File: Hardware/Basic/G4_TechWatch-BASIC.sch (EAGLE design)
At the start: 51 parts, among them J1 FTDI_DEVICESMD, SW1 SWITCH.MOM, SW2 SWITCH.MOM, SW5 SWITCH.MOM, U2 NRF52832_MODULE_MDBT42, U4 PCF8523

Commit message: Board Completed
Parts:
- removed C19: 2.2uF, LinnesLab-Passives:CAPACITOR0402
- removed C20, C21: 4.7u, LinnesLab-Passives:CAPACITOR0603
- removed D4: (no value), LinnesLab-DiscreteSemi:SCHOTTKY-USC
- removed R13, R14, R15: 100k, LinnesLab-Passives:RESISTOR0603
- removed U4: PCF8523, LinnesLab-Clocks:PCF8523
- removed XTAL3: 32.7680kHz, LinnesLab-Clocks:CRYSTALECS-.327-12.5-12-C-TR
- added C1: 1u, LinnesLab-Passives:CAPACITOR0603
- added C3, C4: (no value), LinnesLab-Passives:CAPACITOR0603
- added D3: (no value), LinnesLab-DiscreteSemi:SCHOTTKY-USC
- added R1, R10, R2: 10k, LinnesLab-Passives:RESISTOR0603
- added U1: NRF52832_MODULE_MDBT42, LinnesLab-Microcontrollers:NRF52832_MODULE_MDBT42
- added XTAL1: 32.768kHz, LinnesLab-Clocks:CRYSTALECS-.327-12.5-12-C-TR
- C10: value 300p -> 4.7u
- C11: value 300p -> 100n
- C12: value 10u -> 10uF; device LinnesLab-Passives:CAPACITOR0805 -> LinnesLab-Passives:CAPACITOR0603
- C14: value 100n -> 2.2uF; device LinnesLab-Passives:CAPACITOR0603 -> LinnesLab-Passives:CAPACITOR0402
- C16: value 10uF -> 2.2uF; device LinnesLab-Passives:CAPACITOR0603 -> LinnesLab-Passives:CAPACITOR0402
- C18: value 2.2uF -> 1u; device LinnesLab-Passives:CAPACITOR0402 -> LinnesLab-Passives:CAPACITOR0603
- C2: value 1u -> 10u; device LinnesLab-Passives:CAPACITOR0603 -> LinnesLab-Passives:CAPACITOR0805
- C5, C6: value 1u -> 300p
- C7: value 1u -> 4.7u
- C8, C9: value (none) -> 1u
- R11: value (none) -> 10k
- R12: value 100k -> 390k
- R3: value 1k -> 100k
- R5: value 10k -> 1k
- R6: value 10k -> (none)
- R7: value 390k -> 100k
- R8, R9: value 10k -> 100k
- SW1, SW2: value SWITCH.MOM -> (none); device LinnesLab-Switches:SWITCH.MOM -> LinnesLab-Switches:SPST-PTS830GG140-COPY.1-3
- SW3, SW4: value (none) -> SWITCH.MOM; device LinnesLab-Switches:SPST-PTS830GG140-COPY.1-3 -> LinnesLab-Switches:SWITCH.MOM
- U2: value NRF52832_MODULE_MDBT42 -> PCF8523; device LinnesLab-Microcontrollers:NRF52832_MODULE_MDBT42 -> LinnesLab-Clocks:PCF8523; DIGIKEY (none) -> 568-5306-1-ND; I2C_ADDRESS (none) -> 0x68h; MFN (none) -> PCF8523T/1,118; MFN_MANUFACTURER (none) -> NXP USA Inc.
- XTAL2: value 32.768kHz -> 32.7680kHz; FREQ (none) -> 32.7680KHZ
- renumbered CHRG2 to CHRG1, CORTEX1 to DEBUG1, D5 to D2, L2 to L1, LDO2 to LDO1, LED3 to LED1, LED4 to LED2
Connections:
- net 3.3V: now also C16.2, C18.1, C2.2, C9.1, D3.C, R1.2, R10.2, R2.2, R7.2, U1.VDD; no longer C12.2, C19.2, C2.1, C6.1, D1.C, R15.2, R5.2, R8.2, R9.2, U4.VDD
- net AIN7/BATT: now also R8.1, R9.2, U1.P0.31/AIN7; no longer R13.1, R14.2, U2.P0.31/AIN7
- net CHRG.STAT: now also R3.1, U1.P0.27; no longer R12.1, U2.P0.27
- net CS.OLED: now also U1.P0.16; no longer U2.P0.16
- net D7/SD.CS: now also U1.P0.07; no longer U2.P0.07
- net DC.OLED: now also U1.P0.04/AIN2; no longer U2.P0.04/AIN2
- net DFU: now also SW1.B, U1.P0.20; no longer SW3.B, U2.P0.20
- net DTR: now also C11.1; no longer C14.1
- net FRST: now also U1.P0.22; no longer U2.P0.22
- net GND: now also C1.2, C14.1, C18.2, C2.1, C3.1, C4.2, C5.2, C7.1, R12.2, R7.1, R9.1, SW1.A, SW2.B, SW3.3, SW3.4, SW4.3, SW4.4, U1.GND@1, U1.GND@2, U1.GND@3, U1.GND@4, U2.VSS; no longer C11.2, C18.1, C19.1, C2.2, C20.2, C21.1, C5.1, C7.2, R14.1, R15.1, R7.2, SW1.3, SW1.4, SW2.3, SW2.4, SW3.A, SW4.B, U2.GND@1, U2.GND@2, U2.GND@3, U2.GND@4, U4.VSS
- net LED1: now also R4.2, U1.P0.17; no longer R3.2, U2.P0.17
- net LED2: now also R5.2, U1.P0.19; no longer R4.2, U2.P0.19
- net MISO: now also U1.P0.14; no longer U2.P0.14
- net MOSI: now also U1.P0.13; no longer U2.P0.13
- net N$1: now also R11.2; no longer R6.2
- net N$10: now also R5.1; no longer R4.1
- net N$11: now also U1.DCC; no longer U2.DCC
- net N$12: now also C1.1, U1.DEC4; no longer C7.1, U2.DEC4
- net N$13: now also C12.2; no longer C16.2
- net N$15: now also C14.2; no longer C18.2
- net N$17: now also R6.2; no longer R11.2
- net N$19: now also U2.OSCO, XTAL2.1; no longer U4.OSCO, XTAL3.1
- net N$2: now also R12.1; no longer R7.1
- net N$20: now also U2.OSCI, XTAL2.2; no longer U4.OSCI, XTAL3.2
- net N$3: now also C15.2; no longer C13.2
- net N$4: now also C3.2, U1.P0.00/XL1, XTAL1.1; no longer C8.2, U2.P0.00/XL1, XTAL2.1
- net N$5: now also C15.1; no longer C13.1
- net N$6: now also C4.1, U1.P0.01/XL2, XTAL1.2; no longer C9.1, U2.P0.01/XL2, XTAL2.2
- net N$7: now also C13.2; no longer C15.2
- net N$8: now also C13.1; no longer C15.1
- net N$9: now also R4.1; no longer R3.1
- net P0.09/NFC1: now also C5.1, U1.P0.09; no longer C11.1, U2.P0.09
- net P0.10/NFC2: now also C6.1, U1.P0.10; no longer C10.1, U2.P0.10
- net RESET: now also C11.2, D3.A, R10.1, SW2.A, U1.P0.21/RESET; no longer C14.2, D1.A, R5.1, SW4.A, U2.P0.21/RESET
- net RESET.OLED: now also U1.P0.03/AIN1; no longer U2.P0.03/AIN1
- net RXD: now also U1.P0.08; no longer U2.P0.08
- net SCK: now also U1.P0.12; no longer U2.P0.12
- net SCL: now also R2.1, U1.P0.26, U2.SCL; no longer R8.1, U2.P0.26, U4.SCL
- net SDA: now also R1.1, U1.P0.25, U2.SDA; no longer R9.1, U2.P0.25, U4.SDA
- net SW1: now also SW3.1, SW3.2, U1.P0.11; no longer SW1.1, SW1.2, U2.P0.11
- net SW2: now also SW4.1, SW4.2, U1.P0.15; no longer SW2.1, SW2.2, U2.P0.15
- net SW3: now also U1.P0.28/AIN4; no longer U2.P0.28/AIN4
- net SWCLK: now also U1.SWDCLK; no longer U2.SWDCLK
- net SWDIO: now also U1.SWDIO; no longer U2.SWDIO
- net SWO: now also U1.P0.18/SWO; no longer U2.P0.18/SWO
- net TXD: now also U1.P0.06; no longer U2.P0.06
- net VIN: now also C7.2, C8.2, D1.C, R3.2; no longer C21.2, C5.2, D4.C, R12.2
- net VLIPO: now also C10.1, D1.A, R8.2; no longer C20.1, D4.A, R13.2
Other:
- moved on the sheet: C10, C11, C12, C13, C14, C15, C16, C18, C2, C5, C6, C7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

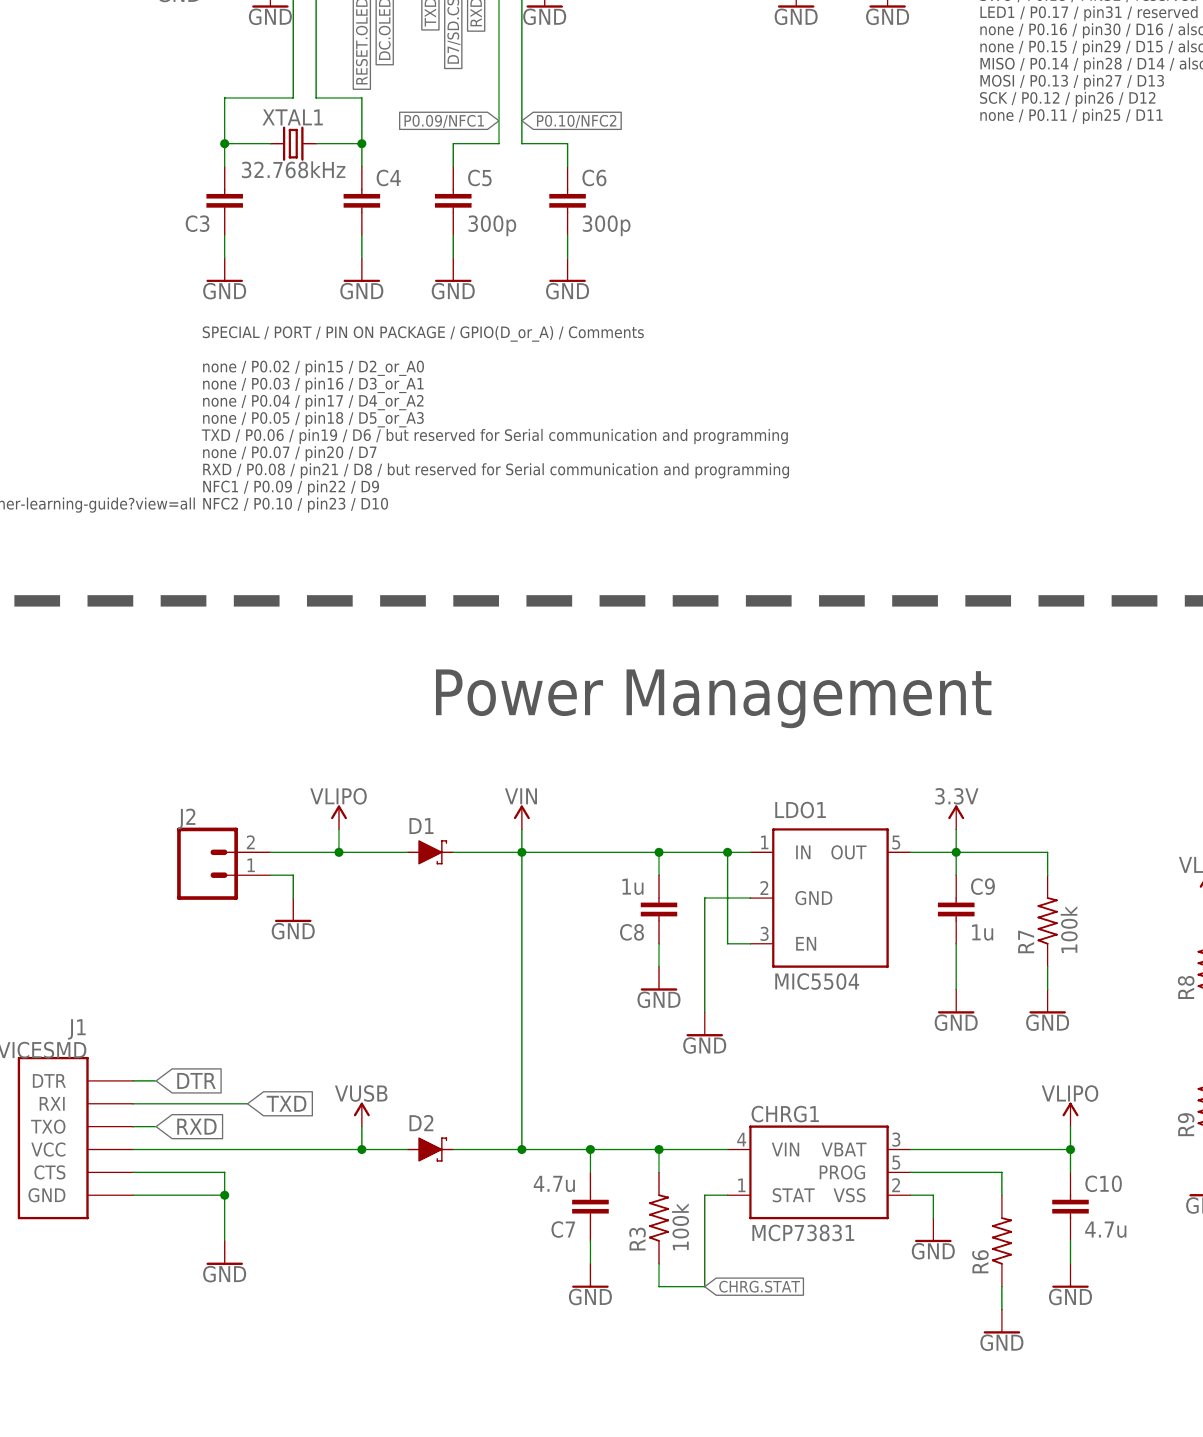
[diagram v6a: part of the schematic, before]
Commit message: Added Missing values, fixed silkscreen and OLED spacing
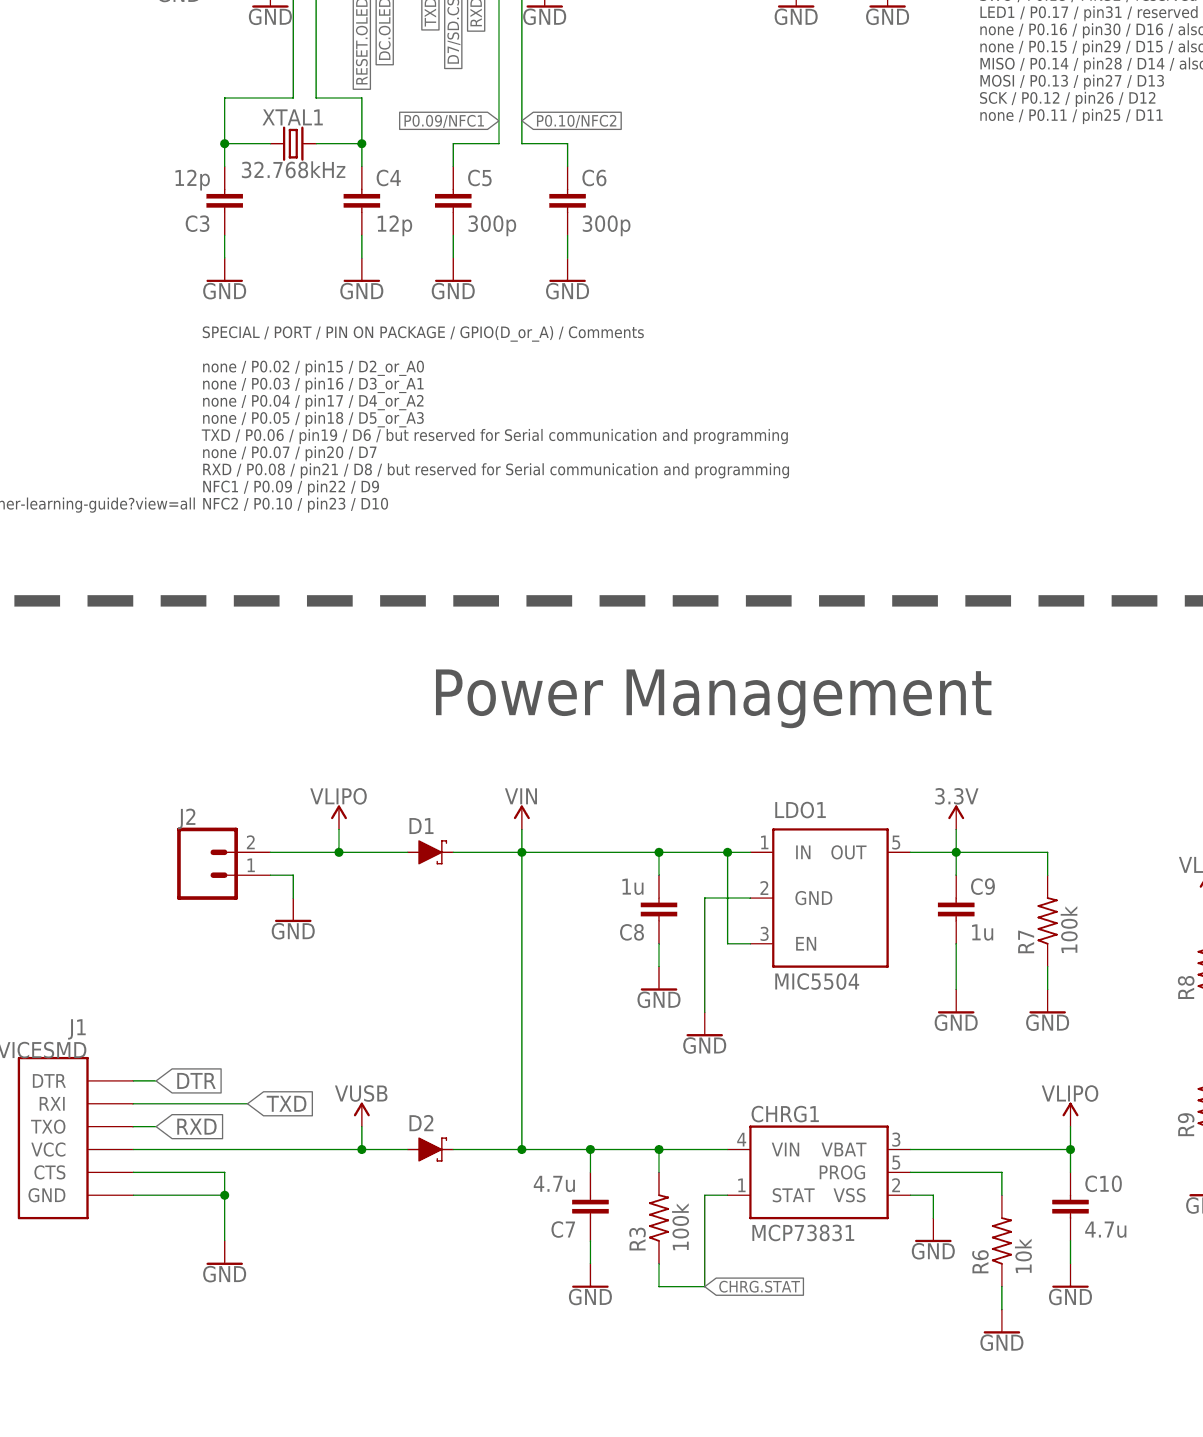
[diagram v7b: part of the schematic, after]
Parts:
- C3, C4: value (none) -> 12p
- R6: value (none) -> 10k
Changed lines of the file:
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@@
 <part name="GND20" library="LinnesLab-Symbols" deviceset="GND" device=""/>
 <part name="C1" library="LinnesLab-Passives" deviceset="CAPACITOR" device="0603" package3d_urn="urn:adsk.eagle:package:15661989/2" value="1u"/>
-<part name="C3" library="LinnesLab-Passives" deviceset="CAPACITOR" device="0603" package3d_urn="urn:adsk.eagle:package:15661989/2"/>
-<part name="C4" library="LinnesLab-Passives" deviceset="CAPACITOR" device="0603" package3d_urn="urn:adsk.eagle:package:15661989/2"/>
+<part name="C3" library="LinnesLab-Passives" deviceset="CAPACITOR" device="0603" package3d_urn="urn:adsk.eagle:package:15661989/2" value="12p"/>
+<part name="C4" library="LinnesLab-Passives" deviceset="CAPACITOR" device="0603" package3d_urn="urn:adsk.eagle:package:15661989/2" value="12p"/>
 <part name="C6" library="LinnesLab-Passives" deviceset="CAPACITOR" device="0603" package3d_urn="urn:adsk.eagle:package:15661989/2" value="300p"/>
 <part name="C5" library="LinnesLab-Passives" deviceset="CAPACITOR" device="0603" package3d_urn="urn:adsk.eagle:package:15661989/2" value="300p"/>
@@
 <part name="C10" library="LinnesLab-Passives" deviceset="CAPACITOR" device="0603" package3d_urn="urn:adsk.eagle:package:15661989/2" value="4.7u"/>
 <part name="C7" library="LinnesLab-Passives" deviceset="CAPACITOR" device="0603" package3d_urn="urn:adsk.eagle:package:15661989/2" value="4.7u"/>
-<part name="R6" library="LinnesLab-Passives" deviceset="RESISTOR" device="0603" package3d_urn="urn:adsk.eagle:package:15661944/2"/>
+<part name="R6" library="LinnesLab-Passives" deviceset="RESISTOR" device="0603" package3d_urn="urn:adsk.eagle:package:15661944/2" value="10k"/>
 <part name="R3" library="LinnesLab-Passives" deviceset="RESISTOR" device="0603" package3d_urn="urn:adsk.eagle:package:15661944/2" value="100k"/>
 <part name="GND34" library="LinnesLab-Symbols" deviceset="GND" device=""/>
